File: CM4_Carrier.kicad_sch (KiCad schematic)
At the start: 8 parts

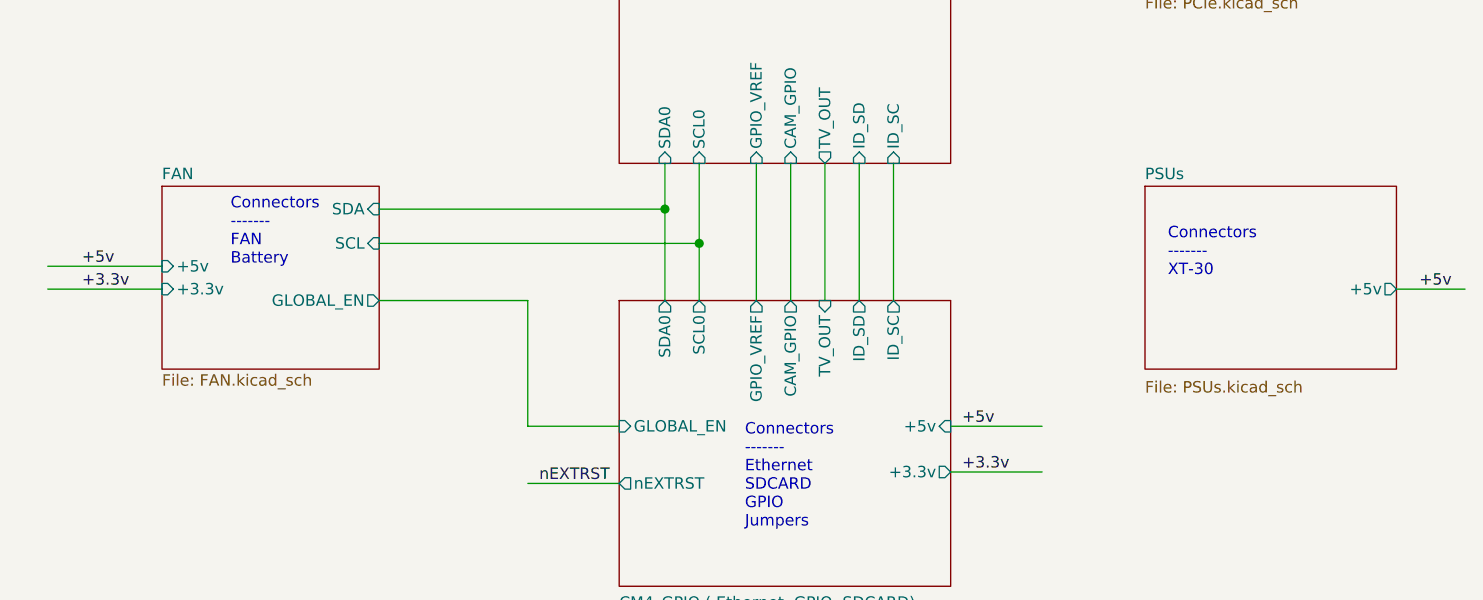
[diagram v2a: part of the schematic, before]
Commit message: starting to lay out switching regulator
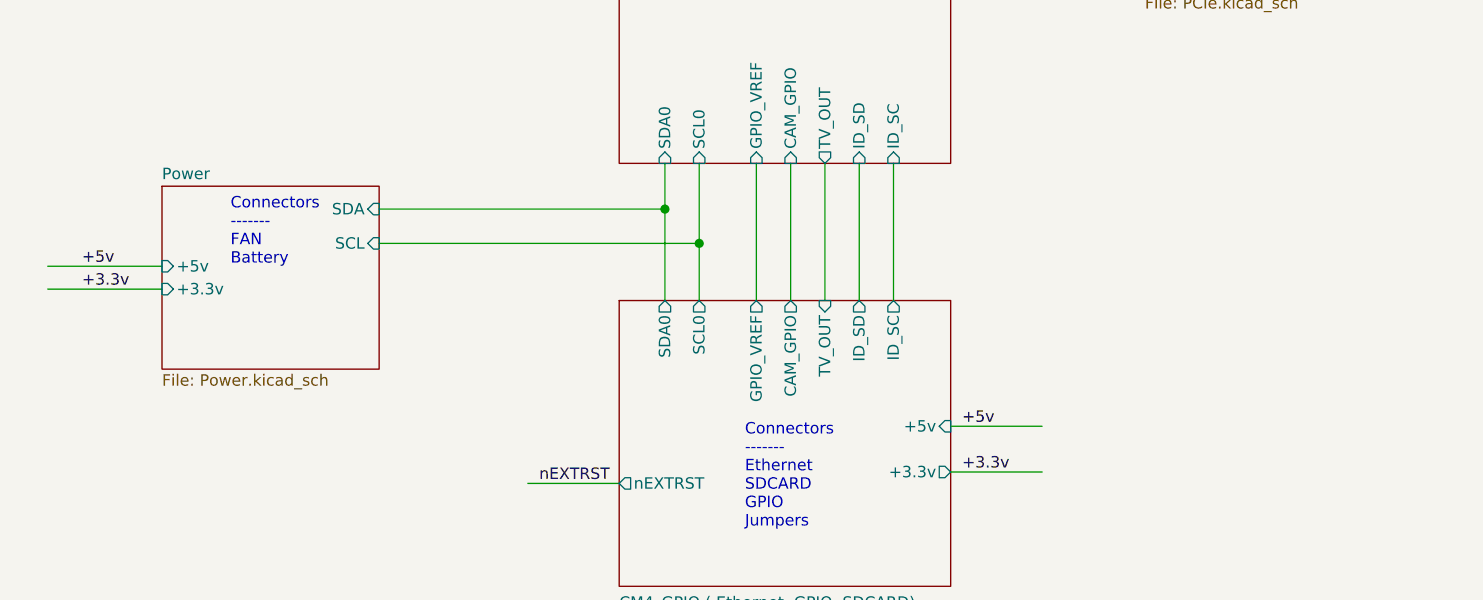
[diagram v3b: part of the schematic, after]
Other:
- sheet FAN renamed Power
- removed sheet PSUs
- sheet CM4_GPIO ( Ethernet, GPIO, SDCARD) ports: added none; removed GLOBAL_EN
- sheet Power: file FAN.kicad_sch -> Power.kicad_sch
- sheet Power ports: added none; removed GLOBAL_EN
- note removed: "Connectors ------- XT-30"

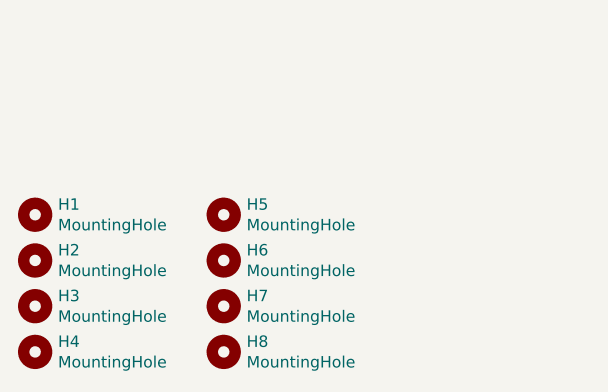
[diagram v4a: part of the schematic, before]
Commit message: started routing USB, added usb power switches, routing some USB-C
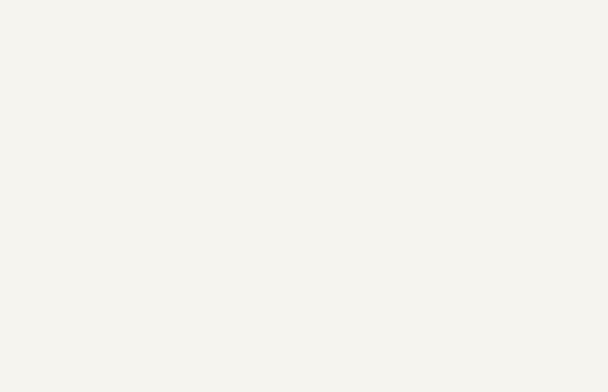
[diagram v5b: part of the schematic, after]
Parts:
- removed H1, H2, H3, H4, H5, H6, H7, H8: MountingHole, MountingHole:MountingHole_2.7mm_M2.5, symbol Mechanical:MountingHole

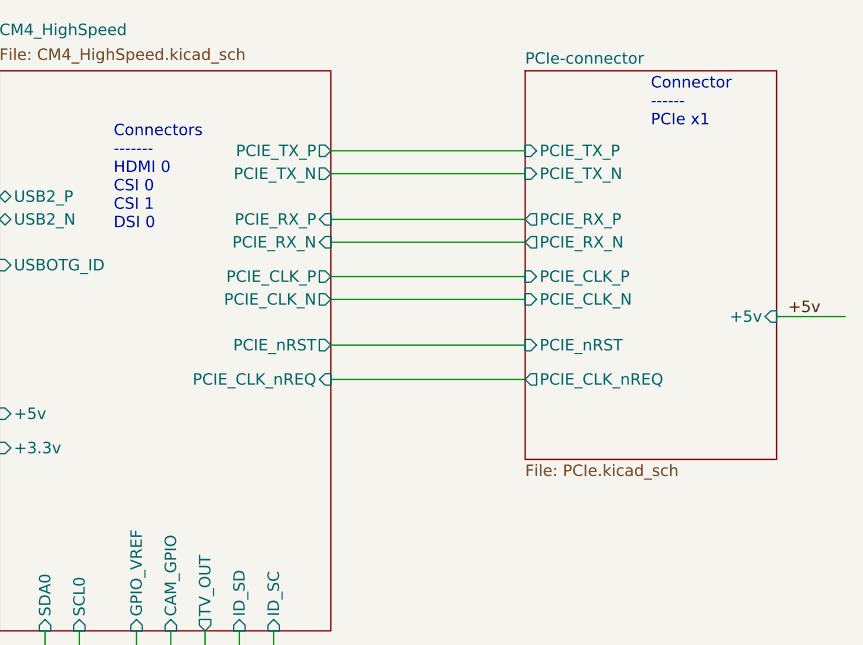
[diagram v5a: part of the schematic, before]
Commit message: lots of changes, added usb power connections, gpio, hdmi, etc
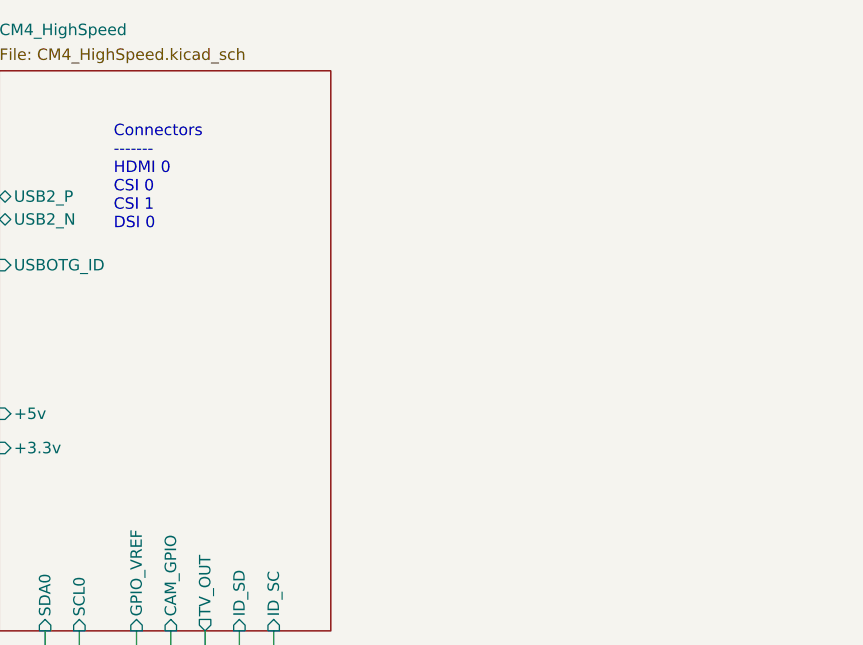
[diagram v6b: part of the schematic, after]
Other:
- removed sheet PCIe-connector
- sheet CM4_HighSpeed ports: added none; removed PCIE_CLK_N, PCIE_CLK_P, PCIE_CLK_nREQ, PCIE_RX_N, PCIE_RX_P, PCIE_TX_N, PCIE_TX_P, PCIE_nRST
- note removed: "Connector ------ PCIe x1"
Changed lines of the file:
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@@
 (kicad_sch (version 20201015) (generator eeschema)
-  (page 1 6)
+  (page 1 5)
   (paper "A4")
   (title_block
@@
     (stroke (width 0) (type solid) (color 0 0 0 0))
   )
-  (wire (pts (xy 168.91 48.26) (xy 190.5 48.26))
-    (stroke (width 0) (type solid) (color 0 0 0 0))
-  )
-  (wire (pts (xy 168.91 50.8) (xy 190.5 50.8))
-    (stroke (width 0) (type solid) (color 0 0 0 0))
-  )
-  (wire (pts (xy 168.91 55.88) (xy 190.5 55.88))
-    (stroke (width 0) (type solid) (color 0 0 0 0))
-  )
-  (wire (pts (xy 168.91 58.42) (xy 190.5 58.42))
-    (stroke (width 0) (type solid) (color 0 0 0 0))
-  )
-  (wire (pts (xy 168.91 62.23) (xy 190.5 62.23))
-    (stroke (width 0) (type solid) (color 0 0 0 0))
-  )
-  (wire (pts (xy 168.91 64.77) (xy 190.5 64.77))
-    (stroke (width 0) (type solid) (color 0 0 0 0))
-  )
-  (wire (pts (xy 168.91 69.85) (xy 190.5 69.85))
-    (stroke (width 0) (type solid) (color 0 0 0 0))
-  )
-  (wire (pts (xy 168.91 73.66) (xy 190.5 73.66))
-    (stroke (width 0) (type solid) (color 0 0 0 0))
-  )
   (wire (pts (xy 168.91 135.89) (xy 179.07 135.89))
     (stroke (width 0) (type solid) (color 0 0 0 0))
@@
     (stroke (width 0) (type solid) (color 0 0 0 0))
   )
-  (wire (pts (xy 218.44 66.675) (xy 226.06 66.675))
-    (stroke (width 0) (type solid) (color 0 0 0 0))
-  )
   (text "Connectors\n-------\nDual USB\nmicroUSB" (at 83.82 49.53 0)
     (effects (font (size 1.27 1.27)) (justify left bottom))
@@
     (effects (font (size 1.27 1.27)) (justify left bottom))
   )
-  (text "Connector\n------\nPCIe x1" (at 204.47 45.72 0)
-    (effects (font (size 1.27 1.27)) (justify left bottom))
-  )
   (label "+5v" (at 72.39 113.03 0)
     (effects (font (size 1.27 1.27)) (justify left bottom))
@@
   )
   (label "+3.3v" (at 170.18 135.89 0)
-    (effects (font (size 1.27 1.27)) (justify left bottom))
-  )
-  (label "+5v" (at 219.71 66.675 0)
     (effects (font (size 1.27 1.27)) (justify left bottom))
   )
@@
       (effects (font (size 1.27 1.27)) (justify left))
     )
-    (pin "PCIE_CLK_P" output (at 168.91 62.23 0)
-      (effects (font (size 1.27 1.27)) (justify right))
-    )
-    (pin "PCIE_CLK_N" output (at 168.91 64.77 0)
-      (effects (font (size 1.27 1.27)) (justify right))
-    )
-    (pin "PCIE_TX_P" output (at 168.91 48.26 0)
-      (effects (font (size 1.27 1.27)) (justify right))
-    )
-    (pin "PCIE_TX_N" output (at 168.91 50.8 0)
-      (effects (font (size 1.27 1.27)) (justify right))
-    )
-    (pin "PCIE_nRST" output (at 168.91 69.85 0)
-      (effects (font (size 1.27 1.27)) (justify right))
-    )
-    (pin "PCIE_RX_P" input (at 168.91 55.88 0)
-      (effects (font (size 1.27 1.27)) (justify right))
-    )
-    (pin "PCIE_RX_N" input (at 168.91 58.42 0)
-      (effects (font (size 1.27 1.27)) (justify right))
-    )
-    (pin "PCIE_CLK_nREQ" input (at 168.91 73.66 0)
-      (effects (font (size 1.27 1.27)) (justify right))
-    )
     (pin "+3.3v" input (at 132.08 81.28 180)
       (effects (font (size 1.27 1.27)) (justify left))
@@
     (pin "TV_OUT" output (at 154.94 101.6 270)
       (effects (font (size 1.27 1.27)) (justify left))
-    )
-  )
-  (sheet (at 190.5 39.37) (size 27.94 43.18)
-    (stroke (width 0.152) (type solid) (color 132 0 132 1))
-    (fill (color 255 255 255 0.0000))
-    (property "Sheet name" "PCIe-connector" (id 0) (at 190.5 38.734 0)
-      (effects (font (size 1.27 1.27)) (justify left bottom))
-    )
-    (property "Sheet file" "PCIe.kicad_sch" (id 1) (at 190.5 83.0585 0)
-      (effects (font (size 1.27 1.27)) (justify left top))
-    )
-    (pin "PCIE_CLK_P" input (at 190.5 62.23 180)
-      (effects (font (size 1.27 1.27)) (justify left))
-    )
-    (pin "PCIE_CLK_N" input (at 190.5 64.77 180)
-      (effects (font (size 1.27 1.27)) (justify left))
-    )
-    (pin "PCIE_TX_P" input (at 190.5 48.26 180)
-      (effects (font (size 1.27 1.27)) (justify left))
-    )
-    (pin "PCIE_TX_N" input (at 190.5 50.8 180)
-      (effects (font (size 1.27 1.27)) (justify left))
-    )
-    (pin "PCIE_CLK_nREQ" output (at 190.5 73.66 180)
-      (effects (font (size 1.27 1.27)) (justify left))
-    )
-    (pin "PCIE_nRST" input (at 190.5 69.85 180)
-      (effects (font (size 1.27 1.27)) (justify left))
-    )
-    (pin "PCIE_RX_P" output (at 190.5 55.88 180)
-      (effects (font (size 1.27 1.27)) (justify left))
-    )
-    (pin "PCIE_RX_N" output (at 190.5 58.42 180)
-      (effects (font (size 1.27 1.27)) (justify left))
-    )
-    (pin "+5v" input (at 218.44 66.675 0)
-      (effects (font (size 1.27 1.27)) (justify right))
     )
   )
@@
     (path "/00000000-0000-0000-0000-00005cff70b1/" (page "4"))
     (path "/00000000-0000-0000-0000-00005cff706a/" (page "5"))
-    (path "/00000000-0000-0000-0000-00005ed4bb5b/" (page "6"))
   )
   (symbol_instances
@@
     )
     (path "/00000000-0000-0000-0000-00005e328d89/6f32a8df-464c-4de5-aca5-3023d8f2b50d"
-      (reference "TP1") (unit 1) (value "TestPoint") (footprint "TestPoint:TestPoint_Pad_2.0x2.0mm")
+      (reference "TP1") (unit 1) (value "TestPoint") (footprint "Connector_PinHeader_2.00mm:PinHeader_1x01_P2.00mm_Vertical")
     )
     (path "/00000000-0000-0000-0000-00005e328d89/75d781f1-0047-4251-8774-f3f189fc3974"
@@
       (reference "J2") (unit 1) (value "Conn_01x22_Female") (footprint "Connector_FFC-FPC:Hirose_FH12-22S-0.5SH_1x22-1MP_P0.50mm_Horizontal")
     )
-    (path "/00000000-0000-0000-0000-00005cff70b1/00000000-0000-0000-0000-00005e67855b"
-      (reference "J6") (unit 1) (value "THD-02-R") (footprint "Connector_PinHeader_2.54mm:PinHeader_2x02_P2.54mm_Vertical")
-    )
     (path "/00000000-0000-0000-0000-00005cff70b1/a0e90fdd-6486-49d4-8aea-5825cf435eec"
       (reference "J8") (unit 1) (value "HDMI_D_1.4") (footprint "Connector_HDMI:HDMI_Micro-D_Molex_46765-0x01")
@@
       (reference "R3") (unit 1) (value "470R") (footprint "Resistor_SMD:R_0402_1005Metric")
     )
-    (path "/00000000-0000-0000-0000-00005cff706a/00000000-0000-0000-0000-00005e5f44e8"
-      (reference "R5") (unit 1) (value "0R") (footprint "Resistor_SMD:R_0805_2012Metric_Pad1.15x1.40mm_HandSolder")
-    )
     (path "/00000000-0000-0000-0000-00005cff706a/00000000-0000-0000-0000-00005e28664f"
       (reference "R10") (unit 1) (value "1k") (footprint "Resistor_SMD:R_0402_1005Metric")
@@
       (reference "U18") (unit 1) (value "RT9742GGJ5") (footprint "Package_TO_SOT_SMD:SOT-23-5")
     )
-    (path "/00000000-0000-0000-0000-00005ed4bb5b/00000000-0000-0000-0000-00005d08bc2b"
-      (reference "#PWR0115") (unit 1) (value "GND") (footprint "")
-    )
-    (path "/00000000-0000-0000-0000-00005ed4bb5b/00000000-0000-0000-0000-00005d338c24"
-      (reference "#PWR0116") (unit 1) (value "GND") (footprint "")
-    )
-    (path "/00000000-0000-0000-0000-00005ed4bb5b/42ae4db4-6840-4fd3-b1a8-00d313d6f619"
-      (reference "J4") (unit 1) (value "2199119-4") (footprint "TE_2199119-4")
-    )
-    (path "/00000000-0000-0000-0000-00005ed4bb5b/00000000-0000-0000-0000-00005ed4ec99"
-      (reference "J12") (unit 1) (value "10018783-11200TLF") (footprint "CM4IO:PCIex1-36")
-    )
-  )
+  )

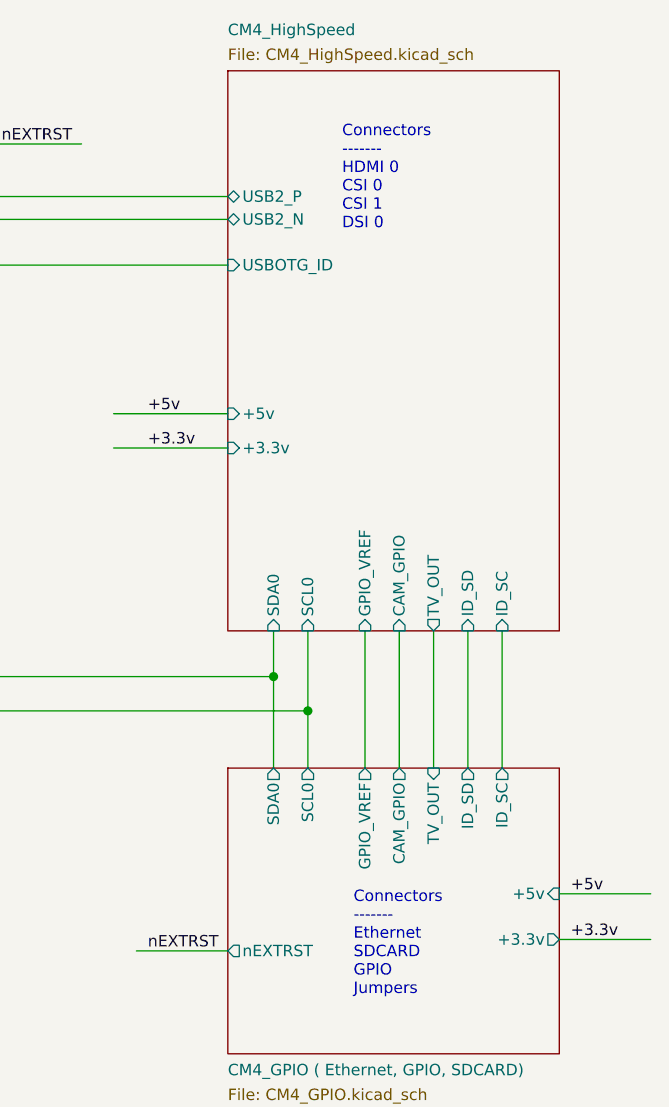
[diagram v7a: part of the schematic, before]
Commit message: additional layout, power circuitry
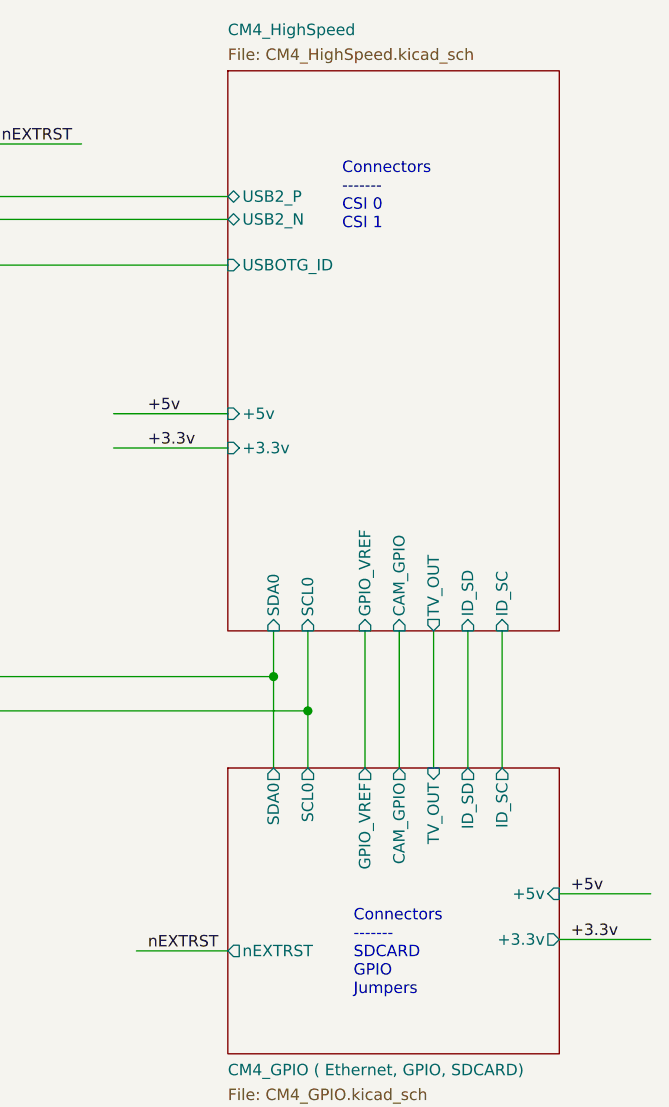
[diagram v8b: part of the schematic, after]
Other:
- note added: "Connectors ------- CSI 0 CSI 1"
- note added: "Connectors ------- SDCARD GPIO Jumpers"
- note removed: "Connectors ------- Ethernet SDCARD GPIO Jumpers"
- note removed: "Connectors ------- HDMI 0 CSI 0 CSI 1 DSI 0"
